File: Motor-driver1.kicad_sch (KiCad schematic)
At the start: 48 parts, among them J8 PINHD_1x4_Male, J9 PINHD_1x4_Male, U2 DRV8825PWP, U3 DRV8825PWP

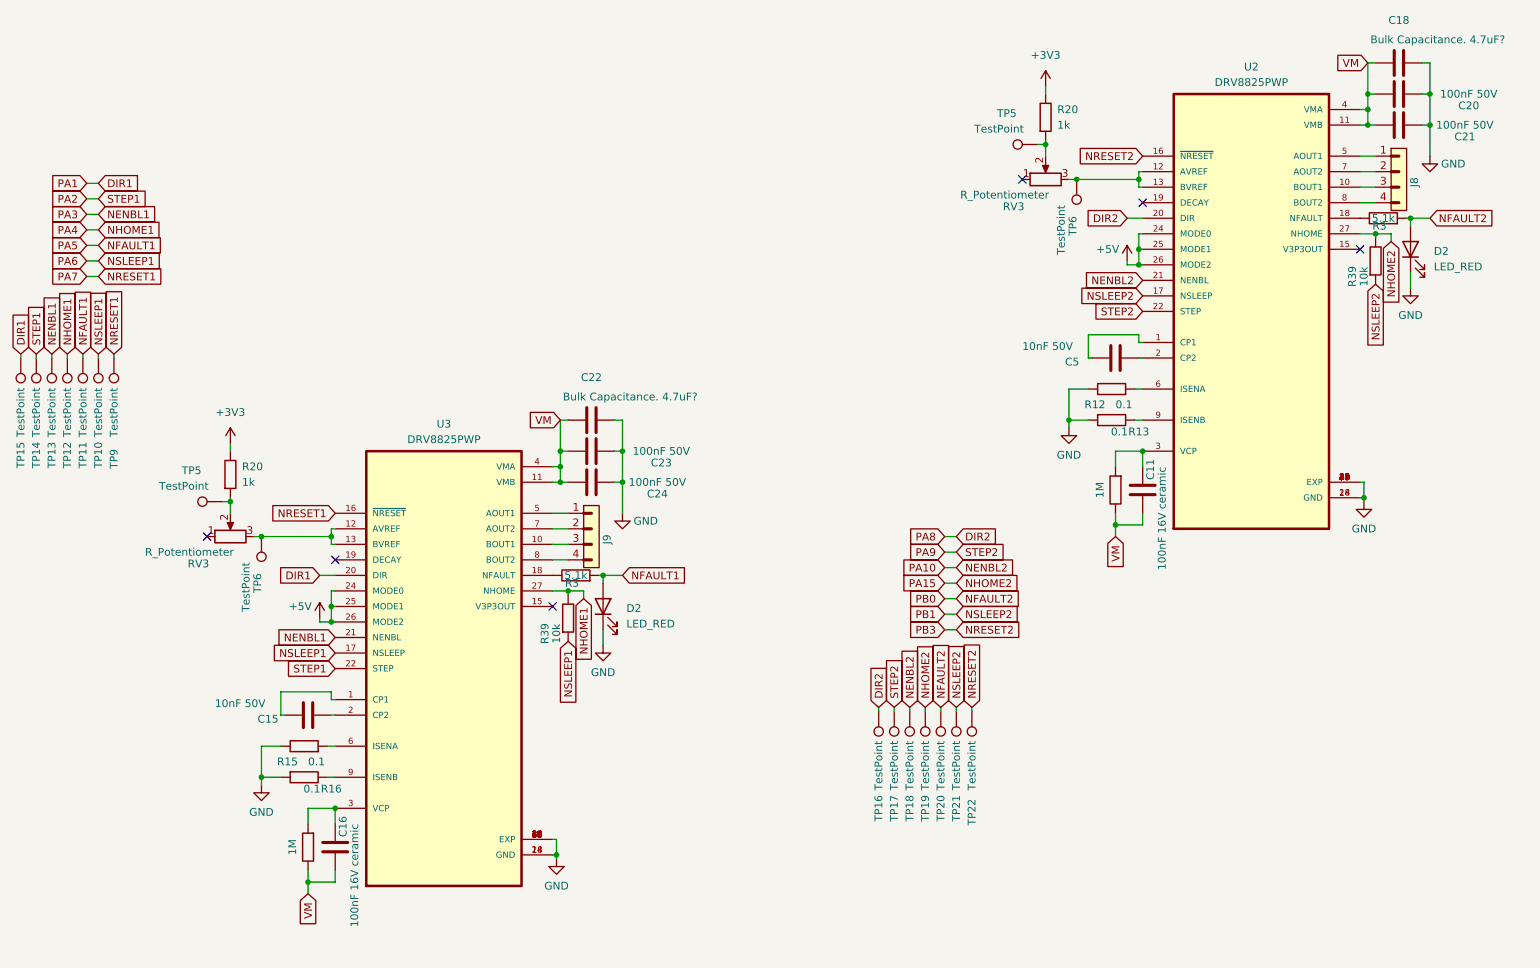
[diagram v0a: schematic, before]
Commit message: deleted unnecessary testpoints
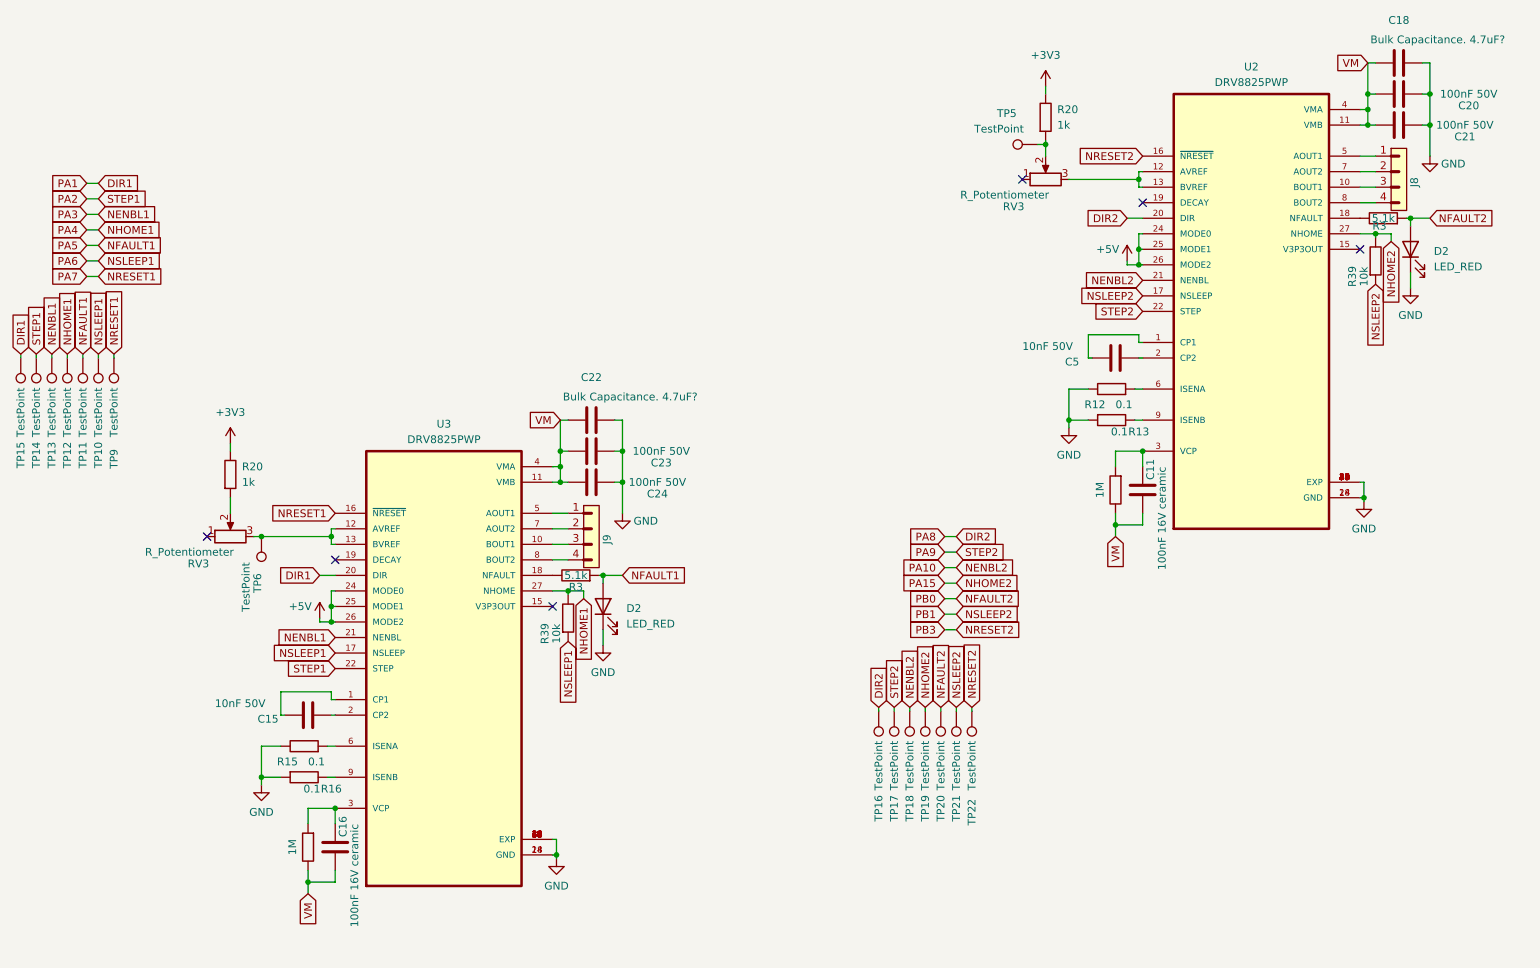
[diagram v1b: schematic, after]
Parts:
- removed TP5, TP6: TestPoint, TestPoint:TestPoint_Pad_D2.5mm, symbol Connector:TestPoint
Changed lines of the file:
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@@
   (junction (at 74.93 151.13) (diameter 0) (color 0 0 0 0)
   )
-  (junction (at 69.85 106.045) (diameter 0) (color 0 0 0 0)
-  )
   (junction (at 123.825 100.33) (diameter 0) (color 0 0 0 0)
   )
   (junction (at 255.27 105.41) (diameter 0) (color 0 0 0 0)
-  )
-  (junction (at 208.28 53.34) (diameter 0) (color 0 0 0 0)
   )
   (junction (at 133.985 102.87) (diameter 0) (color 0 0 0 0)
@@
     (stroke (width 0) (type default))
   )
-  (wire (pts (xy 207.01 53.34) (xy 208.28 53.34))
+  (wire (pts (xy 207.01 53.34) (xy 218.44 53.34))
     (stroke (width 0) (type default))
   )
@@
     (stroke (width 0) (type default))
   )
-  (wire (pts (xy 69.85 106.045) (xy 69.85 107.95))
-    (stroke (width 0) (type default))
-  )
   (wire (pts (xy 266.065 44.45) (xy 266.065 49.53))
     (stroke (width 0) (type default))
@@
     (stroke (width 0) (type default))
   )
-  (wire (pts (xy 208.28 53.34) (xy 218.44 53.34))
-    (stroke (width 0) (type default))
-  )
   (wire (pts (xy 186.69 121.92) (xy 188.595 121.92))
     (stroke (width 0) (type default))
@@
     (stroke (width 0) (type default))
   )
-  (wire (pts (xy 68.58 106.045) (xy 69.85 106.045))
-    (stroke (width 0) (type default))
-  )
   (wire (pts (xy 123.825 102.87) (xy 125.095 102.87))
     (stroke (width 0) (type default))
@@
     (stroke (width 0) (type default))
   )
-  (wire (pts (xy 69.85 105.41) (xy 69.85 106.045))
+  (wire (pts (xy 69.85 105.41) (xy 69.85 107.95))
     (stroke (width 0) (type default))
   )
@@
   (symbol (lib_id "PCM_SL_Devices:Resistor") (at 126.365 118.11 180) (unit 1)
     (in_bom yes) (on_board yes) (dnp no)
-    (property "Reference" "R3" (at 125.73 119.38 0)
+    (property "Reference" "R3" (at 126.365 120.015 0)
       (effects (font (size 1.27 1.27)))
     )
@@
     )
   )
-  (symbol (lib_id "Connector:TestPoint") (at 68.58 106.045 90) (unit 1)
-    (in_bom yes) (on_board yes) (dnp no)
-    (property "Reference" "TP5" (at 63.5 100.965 90)
-      (effects (font (size 1.27 1.27)))
-    )
-    (property "Value" "TestPoint" (at 62.23 103.505 90)
-      (effects (font (size 1.27 1.27)))
-    )
-    (property "Footprint" "TestPoint:TestPoint_Pad_D2.5mm" (at 68.58 100.965 0)
-      (effects (font (size 1.27 1.27)) hide)
-    )
-    (property "Datasheet" "~" (at 68.58 100.965 0)
-      (effects (font (size 1.27 1.27)) hide)
-    )
-    (pin "1")
-    (instances
-      (project "Doodle Drive"
-        (path "/3ec634aa-8c09-482d-9325-2288a4dbd68b/4a4951fa-be57-4d48-97a5-6be750b353b5"
-          (reference "TP5") (unit 1)
-        )
-        (path "/3ec634aa-8c09-482d-9325-2288a4dbd68b/ce40ab82-c304-4dd2-80f5-b6df1964b151"
-          (reference "TP41") (unit 1)
-        )
-      )
-    )
-  )
   (symbol (lib_id "power:+3V3") (at 203.2 38.1 0) (unit 1)
     (in_bom yes) (on_board yes) (dnp no) (fields_autoplaced)
@@
         )
       )
-    )
-  )
-  (symbol (lib_id "Connector:TestPoint") (at 208.28 53.34 180) (unit 1)
-    (in_bom yes) (on_board yes) (dnp no)
-    (property "Reference" "TP6" (at 207.645 60.96 90)
-      (effects (font (size 1.27 1.27)))
-    )
-    (property "Value" "TestPoint" (at 205.74 61.595 90)
-      (effects (font (size 1.27 1.27)))
-    )
-    (property "Footprint" "TestPoint:TestPoint_Pad_D2.5mm" (at 203.2 53.34 0)
-      (effects (font (size 1.27 1.27)) hide)
-    )
-    (property "Datasheet" "~" (at 203.2 53.34 0)
-      (effects (font (size 1.27 1.27)) hide)
-    )
-    (pin "1")
-    (instances
-      (project "Doodle Drive"
-        (path "/3ec634aa-8c09-482d-9325-2288a4dbd68b/4a4951fa-be57-4d48-97a5-6be750b353b5"
-          (reference "TP6") (unit 1)
-        )
-        (path "/3ec634aa-8c09-482d-9325-2288a4dbd68b/ce40ab82-c304-4dd2-80f5-b6df1964b151"
-          (reference "TP2") (unit 1)
-        )
-      )

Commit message: fixed voltage dividers, roughly arrangenged components on pcb, set up 3V3 and GND area
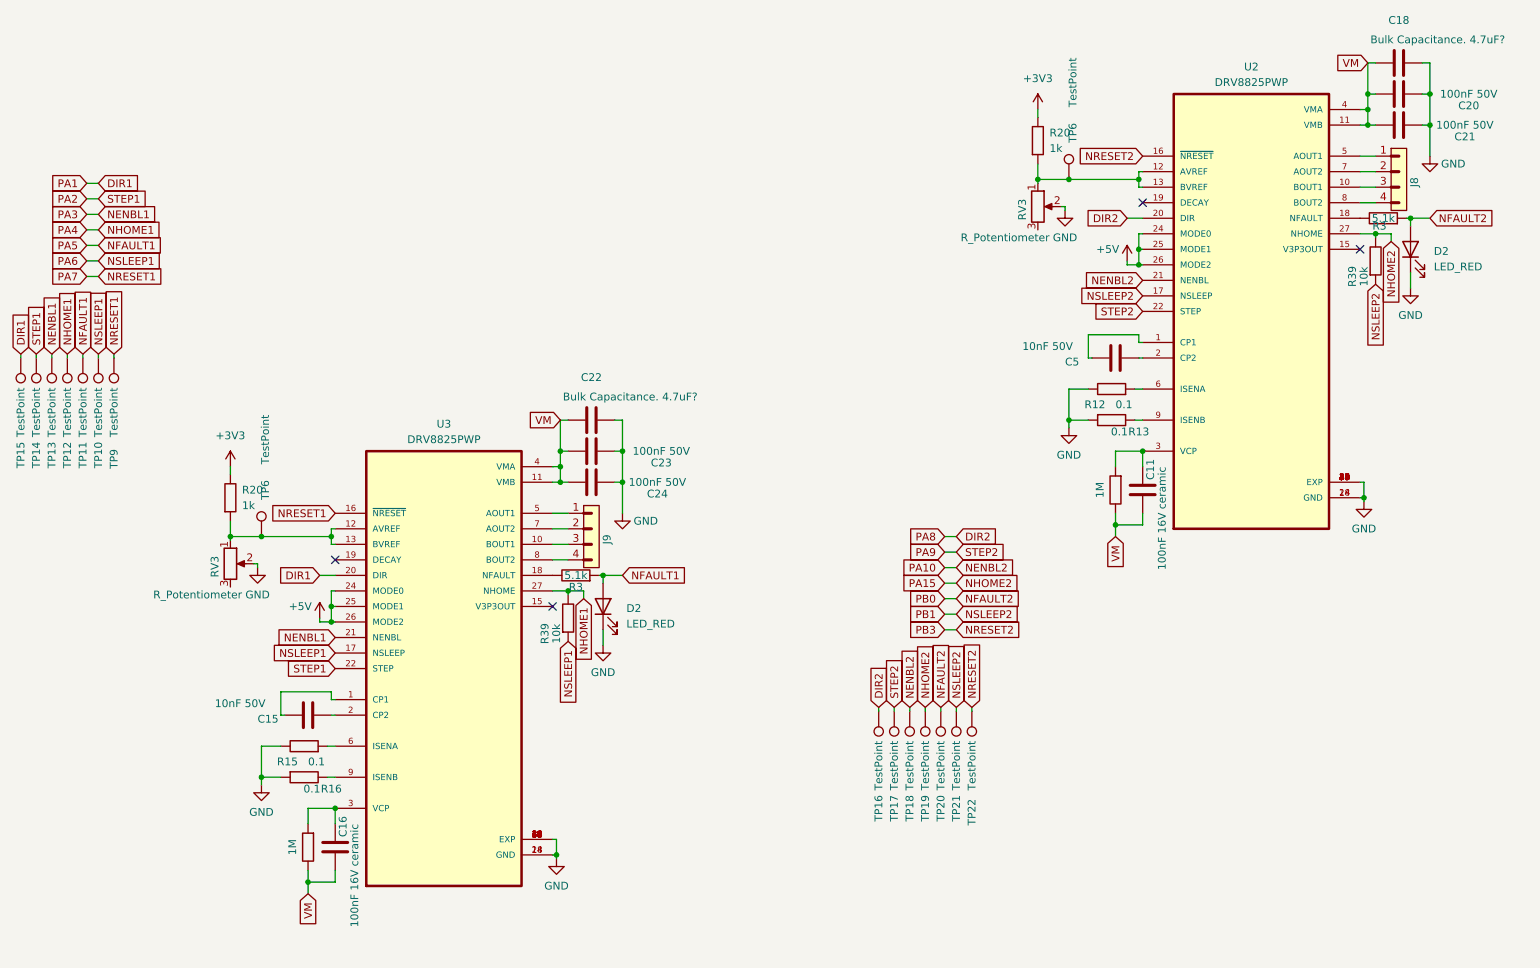
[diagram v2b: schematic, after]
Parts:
- removed TP5: TestPoint, TestPoint:TestPoint_Pad_D2.5mm, symbol Connector:TestPoint
- added TP6: TestPoint, TestPoint:TestPoint_Pad_D2.5mm, symbol Connector:TestPoint
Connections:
- net GND: now also RV3.2, RV3.2
- net at TP6.1, U3.12 (AVREF), U3.13 (BVREF): now also R20.1, RV3.1; no longer RV3.3
- net at RV3.1: now also R20.1, U2.12 (AVREF), U2.13 (BVREF), TP6.1
- now unconnected: RV3.3
- no-connect marks 6 -> 4
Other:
- moved on the sheet: R20, RV3, TP6
